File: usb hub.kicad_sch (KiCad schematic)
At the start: 1 part, among them J1 TYPE-C-31-M-12

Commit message: more updates!
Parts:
- added R1, R2: 5.1k, RMCF0805JT5K10:RESC2012X65N, symbol Device:R
- added USB1, USB2, USB3, USB4: USB_A, symbol Connector:USB_A
- J1: value TYPE-C-31-M-12 -> TYPE_C
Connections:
- net GNDREF: now also R1.1, R2.1, USB1.4 (GND), USB1.5 (Shield), USB2.4 (GND), USB2.5 (Shield), USB3.4 (GND), USB3.5 (Shield), USB4.4 (GND), USB4.5 (Shield)
- net +5V: now reaches J1.A4_B9 (VBUS), J1.B4_A9 (VBUS)
- net at J1.A5 (CC1): now also R2.2
- net USB_DP: now reaches J1.A6 (DP1)
- net USB_DP: now also J1.B6 (DP2)
- net USB_DM: now reaches J1.A7 (DN1)
- net USB_DM: now also J1.B7 (DN2)
- net at J1.B5 (CC2): now also R1.2
- new net D1_N: USB1.2 (D-)
- new net D1_P: USB1.3 (D+)
- new net D2_N: USB2.2 (D-)
- new net D2_P: USB2.3 (D+)
- new net D3_N: USB3.2 (D-)
- new net D3_P: USB3.3 (D+)
- new net D4_N: USB4.2 (D-)
- new net D4_P: USB4.3 (D+)

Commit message: yay sch finito
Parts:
- added D1: R-LED, symbol Device:LED
- added R3, R4, R5: 100ohm, symbol Device:R
- added R6: 2.7k ohm, symbol Device:R
- added U1: FE1.1s, Package_SO:SSOP-28_3.9x9.9mm_P0.635mm, symbol Interface_USB:FE1.1s
- added USB_1, USB_2, USB_3, USB_4: G-LED, symbol Device:LED
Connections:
- net +5V: now also USB1.1 (VBUS), USB2.1 (VBUS), USB3.1 (VBUS), USB4.1 (VBUS), U1.20 (VDD5)
- net D1_N: now also U1.10 (DM1)
- net D1_P: now also U1.11 (DP1)
- net D2_N: now also U1.8 (DM2)
- net D2_P: now also U1.9 (DP2)
- net D3_N: now also U1.6 (DM3)
- net D3_P: now also U1.7 (DP3)
- net D4_N: now also U1.4 (DM4)
- net D4_P: now also U1.5 (DP4)
- net GNDREF: now also R3.1, R6.2, U1.1 (VSS), USB_1.2 (A), USB_2.2 (A), USB_3.1 (K), USB_4.1 (K)
- net USB_DM: now also U1.15 (DMU)
- net USB_DP: now also U1.16 (DPU)
- new net: R5.1, U1.24 (LED2)
- new net: R5.2, USB_2.1 (K), USB_4.2 (A)
- new net: R4.1, USB_1.1 (K), USB_3.2 (A)
- new net: R4.2, U1.23 (LED1/EESCL)
- new net: D1.1 (K), R3.2
- new net: R6.1, U1.14 (REXT)
- new net: D1.2 (A), U1.22 (DRV)
- new net +3.3V: U1.13 (VD33), U1.17 (~{XRSTJ}), U1.19 (BUSJ), U1.21 (VD33_O)
- no-connect marks 0 -> 6

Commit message: a bit of part placemnt
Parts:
- added C1, C2, C3, C4, C5: 10uf, Capacitor_SMD:C_0201_0603Metric, symbol Device:C_Small
- J1: footprint TYPE-C-31-M-12:HRO_TYPE-C-31-M-12 -> Connector_USB:USB_C_Receptacle_HRO_TYPE-C-31-M-12
- PWR1: renamed from D1; footprint (none) -> Diode_SMD:D_0201_0603Metric
- R1, R2: footprint RMCF0805JT5K10:RESC2012X65N -> Resistor_SMD:R_01005_0402Metric
- R3, R4, R5, R6: footprint (none) -> Resistor_SMD:R_0201_0603Metric
- USB1, USB2, USB3, USB4: footprint (none) -> Connector_USB:USB_A_Receptacle_GCT_USB1046
- USB_1, USB_2, USB_3, USB_4: footprint (none) -> Diode_SMD:D_0201_0603Metric
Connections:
- net +5V: now also C1.2, C2.2, C3.2, C4.2
- net GNDREF: now also C1.1, C2.1, C3.1, C4.1, C5.1
- net at U1.12 (VD18_O): now also U1.28 (VD18), C5.2
- no-connect marks 6 -> 4

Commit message: all routes fixed AND placed parts
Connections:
- net +5V: now also J1.A4 (VBUS), J1.A9 (VBUS), J1.B4 (VBUS), J1.B9 (VBUS); no longer J1.A4_B9 (VBUS), J1.B4_A9 (VBUS)
- net GNDREF renamed GND
- net GND: now also J1.A1 (GND), J1.A12 (GND), J1.B1 (GND), J1.B12 (GND); no longer J1.A1_B12 (GND), J1.B1_A12 (GND)
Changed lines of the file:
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@@
 		(pin "S4"
 		)
-		(pin "B4_A9"
+		(pin "B1"
 		)
 		(pin "B6"
 		)
-		(pin "B1_A12"
+		(pin "A4"
 		)
 		(pin "A5"
@@
 		(pin "A7"
 		)
-		(pin "A1_B12"
+		(pin "B12"
 		)
 		(pin "A8"
@@
 		(pin "S1"
 		)
-		(pin "A4_B9"
+		(pin "A9"
 		)
 		(pin "B5"
@@
 		(pin "B7"
 		)
+		(pin "A12"
+		)
+		(pin "A1"
+		)
+		(pin "B9"
+		)
+		(pin "B4"
+		)
 		(instances

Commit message: bit of routing
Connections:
- net GND: now also PWR1.1 (K); no longer R3.1
- net at R3.2: now also U1.22 (DRV); no longer PWR1.1 (K)
- net at PWR1.2 (A): now also R3.1; no longer U1.22 (DRV)
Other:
- moved on the sheet: PWR1, R6
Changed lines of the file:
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@@
 	)
 	(junction
-		(at 123.19 100.33)
-		(diameter 0)
-		(color 0 0 0 0)
-	)
-	(junction
 		(at 121.92 160.02)
 		(diameter 0)
@@
 	)
 	(junction
+		(at 123.19 99.06)
+		(diameter 0)
+		(color 0 0 0 0)
+	)
+	(junction
 		(at 88.9 114.3)
 		(diameter 0)
@@
 	(wire
 		(pts
-			(xy 97.79 113.03) (xy 97.79 114.3)
+			(xy 44.45 82.55) (xy 46.99 82.55)
 		)
 		(stroke
@@
 	(wire
 		(pts
-			(xy 44.45 82.55) (xy 46.99 82.55)
+			(xy 140.97 149.86) (xy 142.24 149.86)
 		)
 		(stroke
@@
 	(wire
 		(pts
-			(xy 140.97 149.86) (xy 142.24 149.86)
+			(xy 97.79 99.06) (xy 123.19 99.06)
 		)
 		(stroke
@@
 	(wire
 		(pts
-			(xy 97.79 105.41) (xy 97.79 100.33)
-		)
-		(stroke
-			(width 0)
-			(type default)
-		)
-	)
-	(wire
-		(pts
 			(xy 88.9 127) (xy 88.9 119.38)
 		)
@@
 	(wire
 		(pts
-			(xy 140.97 100.33) (xy 140.97 109.22)
+			(xy 140.97 99.06) (xy 140.97 109.22)
 		)
 		(stroke
@@
 	(wire
 		(pts
-			(xy 78.105 112.395) (xy 81.28 112.395)
+			(xy 123.19 99.06) (xy 123.19 104.14)
 		)
 		(stroke
@@
 	(wire
 		(pts
-			(xy 123.19 97.79) (xy 123.19 100.33)
+			(xy 78.105 112.395) (xy 81.28 112.395)
 		)
 		(stroke
@@
 	(wire
 		(pts
-			(xy 106.68 100.33) (xy 123.19 100.33)
+			(xy 123.19 97.79) (xy 123.19 99.06)
 		)
 		(stroke
@@
 	(wire
 		(pts
-			(xy 133.35 100.33) (xy 123.19 100.33)
+			(xy 133.35 99.06) (xy 123.19 99.06)
 		)
 		(stroke
@@
 	(wire
 		(pts
-			(xy 123.19 100.33) (xy 123.19 104.14)
-		)
-		(stroke
-			(width 0)
-			(type default)
-		)
-	)
-	(wire
-		(pts
 			(xy 128.27 162.56) (xy 128.27 160.02)
 		)
@@
 	(wire
 		(pts
-			(xy 97.79 100.33) (xy 99.06 100.33)
-		)
-		(stroke
-			(width 0)
-			(type default)
-		)
-	)
-	(wire
-		(pts
 			(xy 72.39 82.55) (xy 74.93 82.55)
 		)
@@
 	)
 	(symbol
-		(lib_id "Device:R")
-		(at 102.87 100.33 270)
-		(unit 1)
-		(exclude_from_sim no)
-		(in_bom yes)
-		(on_board yes)
-		(dnp no)
-		(fields_autoplaced yes)
-		(property "Reference" "R3"
-			(at 102.87 93.98 90)
-			(effects
-				(font
-					(size 1.27 1.27)
-				)
-			)
-		)
-		(property "Value" "100ohm"
-			(at 102.87 96.52 90)
-			(effects
-				(font
-					(size 1.27 1.27)
-				)
-			)
-		)
-		(property "Footprint" "Resistor_SMD:R_0201_0603Metric"
-			(at 102.87 98.552 90)
-			(effects
-				(font
-					(size 1.27 1.27)
-				)
-				(hide yes)
-			)
-		)
-		(property "Datasheet" "~"
-			(at 102.87 100.33 0)
-			(effects
-				(font
-					(size 1.27 1.27)
-				)
-				(hide yes)
-			)
-		)
-		(property "Description" "Resistor"
-			(at 102.87 100.33 0)
-			(effects
-				(font
-					(size 1.27 1.27)
-				)
-				(hide yes)
-			)
-		)
-		(pin "1"
-		)
-		(pin "2"
-		)
-		(instances
-			(project ""
-				(path "/d6e9f345-7462-4a5d-9cb3-9d4e9bb08c51"
-					(reference "R3")
-					(unit 1)
-				)
-			)
-		)
-	)
-	(symbol
 		(lib_id "Connector:USB_A")
 		(at 46.99 45.72 0)
@@
 	)
 	(symbol
+		(lib_id "Device:R")
+		(at 97.79 110.49 0)
+		(unit 1)
+		(exclude_from_sim no)
+		(in_bom yes)
+		(on_board yes)
+		(dnp no)
+		(fields_autoplaced yes)
+		(property "Reference" "R3"
+			(at 100.33 109.2199 0)
+			(effects
+				(font
+					(size 1.27 1.27)
+				)
+				(justify left)
+			)
+		)
+		(property "Value" "100ohm"
+			(at 100.33 111.7599 0)
+			(effects
+				(font
+					(size 1.27 1.27)
+				)
+				(justify left)
+			)
+		)
+		(property "Footprint" "Resistor_SMD:R_0201_0603Metric"
+			(at 96.012 110.49 90)
+			(effects
+				(font
+					(size 1.27 1.27)
+				)
+				(hide yes)
+			)
+		)
+		(property "Datasheet" "~"
+			(at 97.79 110.49 0)
+			(effects
+				(font
+					(size 1.27 1.27)
+				)
+				(hide yes)
+			)
+		)
+		(property "Description" "Resistor"
+			(at 97.79 110.49 0)
+			(effects
+				(font
+					(size 1.27 1.27)
+				)
+				(hide yes)
+			)
+		)
+		(pin "1"
+		)
+		(pin "2"
+		)
+		(instances
+			(project "usb hub"
+				(path "/d6e9f345-7462-4a5d-9cb3-9d4e9bb08c51"
+					(reference "R3")
+					(unit 1)
+				)
+			)
+		)
+	)
+	(symbol
 		(lib_id "power:GNDREF")
 		(at 82.55 62.23 180)
@@
 	(symbol
 		(lib_id "Device:R")
-		(at 137.16 100.33 270)
+		(at 137.16 99.06 270)
 		(unit 1)
 		(exclude_from_sim no)
@@
 		(dnp no)
 		(property "Reference" "R6"
-			(at 137.16 95.504 90)
+			(at 137.16 94.234 90)
 			(effects
 				(font
@@
 		)
 		(property "Value" "2.7k ohm"
-			(at 137.16 98.044 90)
+			(at 137.16 96.774 90)
 			(effects
 				(font
@@
 		)
 		(property "Footprint" "Resistor_SMD:R_0201_0603Metric"
-			(at 137.16 98.552 90)
+			(at 137.16 97.282 90)
 			(effects
 				(font
@@
 		)
 		(property "Datasheet" "~"
-			(at 137.16 100.33 0)
+			(at 137.16 99.06 0)
 			(effects
 				(font
@@
 		)
 		(property "Description" "Resistor"
-			(at 137.16 100.33 0)
+			(at 137.16 99.06 0)
 			(effects
 				(font
@@
 	(symbol
 		(lib_id "Device:LED")
-		(at 97.79 109.22 270)
+		(at 97.79 102.87 270)
 		(unit 1)
 		(exclude_from_sim no)
@@
 		(on_board yes)
 		(dnp no)
-		(fields_autoplaced yes)
 		(property "Reference" "PWR1"
-			(at 100.33 106.3624 90)
+			(at 100.33 100.0124 90)
 			(effects
 				(font
@@
 		)
 		(property "Value" "R-LED"
-			(at 100.33 108.9024 90)
+			(at 100.33 102.5524 90)
 			(effects
 				(font
@@
 		)
 		(property "Footprint" "Diode_SMD:D_0201_0603Metric"
-			(at 97.79 109.22 0)
+			(at 97.79 102.87 0)
 			(effects
 				(font
@@
 		)
 		(property "Datasheet" "~"
-			(at 97.79 109.22 0)
+			(at 97.79 102.87 0)
 			(effects
 				(font
@@
 		)
 		(property "Description" "Light emitting diode"
-			(at 97.79 109.22 0)
+			(at 97.79 102.87 0)
 			(effects
 				(font

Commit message: aaaaaaaaa
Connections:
- net at C5.2, U1.12 (VD18_O): no longer U1.28 (VD18)
- no-connect marks 4 -> 5
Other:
- moved on the sheet: C5
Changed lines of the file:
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@@
 	)
 	(junction
-		(at 115.57 160.02)
-		(diameter 0)
-		(color 0 0 0 0)
-	)
-	(junction
 		(at 82.55 40.64)
 		(diameter 0)
@@
 	)
 	(no_connect
+		(at 115.57 160.02)
+	)
+	(no_connect
 		(at 140.97 154.94)
 	)
@@
 	(wire
 		(pts
-			(xy 115.57 160.02) (xy 118.11 160.02)
-		)
-		(stroke
-			(width 0)
-			(type default)
-		)
-	)
-	(wire
-		(pts
 			(xy 88.9 130.81) (xy 88.9 127)
 		)
@@
 	(symbol
 		(lib_id "power:GNDREF")
-		(at 115.57 165.1 0)
+		(at 118.11 165.1 0)
 		(unit 1)
 		(exclude_from_sim no)
@@
 		(dnp no)
 		(property "Reference" "#PWR022"
-			(at 115.57 171.45 0)
+			(at 118.11 171.45 0)
 			(effects
 				(font
@@
 		)
 		(property "Value" "GNDREF"
-			(at 115.316 168.402 0)
+			(at 117.856 168.402 0)
 			(effects
 				(font
@@
 		)
 		(property "Footprint" ""
-			(at 115.57 165.1 0)
+			(at 118.11 165.1 0)
 			(effects
 				(font
@@
 		)
 		(property "Datasheet" ""
-			(at 115.57 165.1 0)
+			(at 118.11 165.1 0)
 			(effects
 				(font
@@
 		)
 		(property "Description" ""
-			(at 115.57 165.1 0)
+			(at 118.11 165.1 0)
 			(effects
 				(font
@@
 	(symbol
 		(lib_id "Device:C_Small")
-		(at 115.57 162.56 180)
+		(at 118.11 162.56 180)
 		(unit 1)
 		(exclude_from_sim no)
@@
 		(fields_autoplaced yes)
 		(property "Reference" "C5"
-			(at 113.03 163.8238 0)
+			(at 115.57 163.8238 0)
 			(effects
 				(font
@@
 		)
 		(property "Value" "10uf"
-			(at 113.03 161.2838 0)
+			(at 115.57 161.2838 0)
 			(effects
 				(font
@@
 		)
 		(property "Footprint" "Capacitor_SMD:C_0201_0603Metric"
-			(at 115.57 162.56 0)
+			(at 118.11 162.56 0)
 			(effects
 				(font
@@
 		)
 		(property "Datasheet" "~"
-			(at 115.57 162.56 0)
+			(at 118.11 162.56 0)
 			(effects
 				(font
@@
 		)
 		(property "Description" "Unpolarized capacitor, small symbol"
-			(at 115.57 162.56 0)
+			(at 118.11 162.56 0)
 			(effects
 				(font

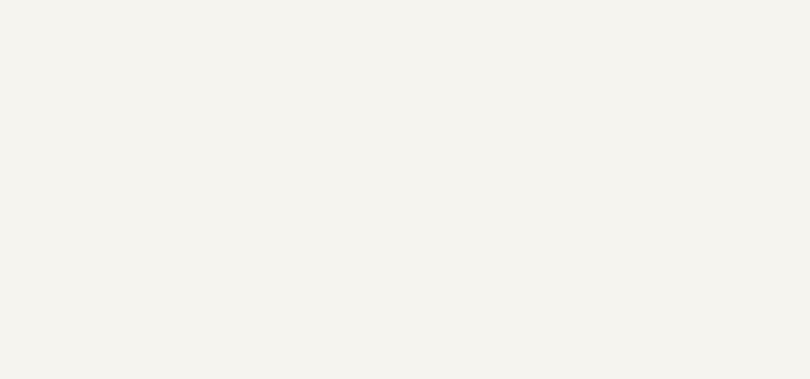
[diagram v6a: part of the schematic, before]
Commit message: fixed some sch stuff, need to add holes still
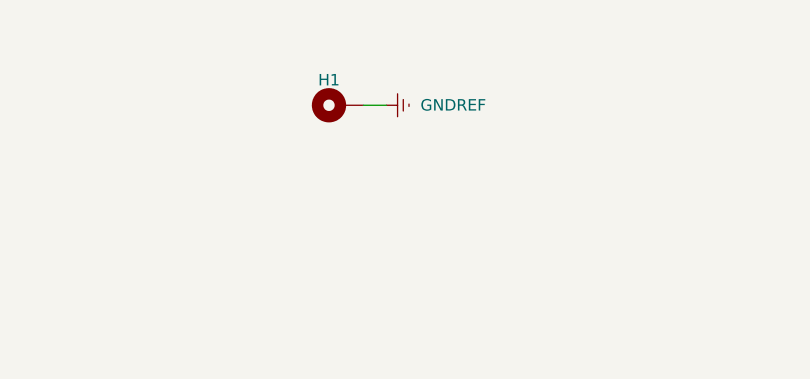
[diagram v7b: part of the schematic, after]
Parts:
- added H1: MountingHole_Pad, MountingHole:MountingHole_2.2mm_M2_Pad_TopBottom, symbol Mechanical:MountingHole_Pad
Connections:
- net GND: now also H1.1
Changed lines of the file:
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@@
 	(wire
 		(pts
+			(xy 149.86 40.64) (xy 152.4 40.64)
+		)
+		(stroke
+			(width 0)
+			(type default)
+		)
+	)
+	(wire
+		(pts
 			(xy 88.9 127) (xy 88.9 119.38)
 		)
@@
 	)
 	(symbol
+		(lib_id "power:GNDREF")
+		(at 152.4 40.64 90)
+		(unit 1)
+		(exclude_from_sim no)
+		(in_bom yes)
+		(on_board yes)
+		(dnp no)
+		(fields_autoplaced yes)
+		(property "Reference" "#PWR023"
+			(at 158.75 40.64 0)
+			(effects
+				(font
+					(size 1.27 1.27)
+				)
+				(hide yes)
+			)
+		)
+		(property "Value" "GNDREF"
+			(at 156.21 40.6399 90)
+			(effects
+				(font
+					(size 1.27 1.27)
+				)
+				(justify right)
+			)
+		)
+		(property "Footprint" ""
+			(at 152.4 40.64 0)
+			(effects
+				(font
+					(size 1.27 1.27)
+				)
+				(hide yes)
+			)
+		)
+		(property "Datasheet" ""
+			(at 152.4 40.64 0)
+			(effects
+				(font
+					(size 1.27 1.27)
+				)
+				(hide yes)
+			)
+		)
+		(property "Description" "Power symbol creates a global label with name \"GNDREF\" , reference supply ground"
+			(at 152.4 40.64 0)
+			(effects
+				(font
+					(size 1.27 1.27)
+				)
+				(hide yes)
+			)
+		)
+		(pin "1"
+		)
+		(instances
+			(project "usb hub"
+				(path "/d6e9f345-7462-4a5d-9cb3-9d4e9bb08c51"
+					(reference "#PWR023")
+					(unit 1)
+				)
+			)
+		)
+	)
+	(symbol
 		(lib_id "Device:LED")
 		(at 85.09 127 0)
@@
 					(unit 1)
 				)
+			)
+		)
+	)
+	(symbol
+		(lib_id "Mechanical:MountingHole_Pad")
+		(at 147.32 40.64 90)
+		(unit 1)
+		(exclude_from_sim yes)
+		(in_bom no)
+		(on_board yes)
+		(dnp no)
+		(property "Reference" "H1"
+			(at 146.05 37.846 90)
+			(effects
+				(font
+					(size 1.27 1.27)
+				)
+			)
+		)
+		(property "Value" "MountingHole_Pad"
+			(at 146.05 36.83 90)
+			(effects
+				(font
+					(size 1.27 1.27)
+				)
+				(hide yes)
+			)
+		)
+		(property "Footprint" "MountingHole:MountingHole_2.2mm_M2_Pad_TopBottom"
+			(at 147.32 40.64 0)
+			(effects
+				(font
+					(size 1.27 1.27)
+				)
+				(hide yes)
+			)
+		)
+		(property "Datasheet" "~"
+			(at 147.32 40.64 0)
+			(effects
+				(font
+					(size 1.27 1.27)
+				)
+				(hide yes)
+			)
+		)
+		(property "Description" "Mounting Hole with connection"
+			(at 147.32 40.64 0)
+			(effects
+				(font
+					(size 1.27 1.27)
+				)
+				(hide yes)
+			)
+		)
+		(pin "1"
+		)
+		(instances
+			(project "usb hub"
+				(path "/d6e9f345-7462-4a5d-9cb3-9d4e9bb08c51"
+					(reference "H1")
+					(unit 1)
+				)
